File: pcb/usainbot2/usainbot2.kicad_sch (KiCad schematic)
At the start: 13 parts, among them J1 BT_MOD, J2 QTR1-L, J3 QTR1-R, J4 QTR8, J5 SWITCH, M1 Conn_01x02_Male, M2 Conn_01x02_Male, SW1 BTN1, SW2 BTN2

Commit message: update pcb, falta rutear
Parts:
- removed J4: QTR8, Connector_PinSocket_2.54mm:PinSocket_1x11_P2.54mm_Horizontal, symbol usainbot2-rescue:Conn_01x11_Female-Connector
- removed J5: SWITCH, Connector_PinHeader_2.54mm:PinHeader_1x03_P2.54mm_Vertical, symbol usainbot2-rescue:Conn_01x03_Female-Connector
- removed SW1: BTN1, Button_Switch_THT:SW_PUSH_6mm, symbol Switch:SW_MEC_5E
- added C1, C2: C, Capacitor_SMD:C_0805_2012Metric_Pad1.18x1.45mm_HandSolder, symbol Device:C
- added D1: WS2812B, LED_SMD:LED_WS2812B_PLCC4_5.0x5.0mm_P3.2mm, symbol LED:WS2812B
- added J4: QTR-6A, Connector_PinHeader_2.54mm:PinHeader_1x09_P2.54mm_Horizontal, symbol Connector:Conn_01x09_Female
- added SW1: SW_SPDT, usainbot:TOGGLE_RA, symbol Switch:SW_SPDT
- added U2: LM7805_TO220, Package_TO_SOT_THT:TO-220-3_Vertical, symbol Regulator_Linear:LM7805_TO220
- BATTJ6: footprint Connector_PinHeader_2.54mm:PinHeader_1x02_P2.54mm_Horizontal -> Connector_Molex:Molex_KK-254_AE-6410-02A_1x02_P2.54mm_Vertical
- J2, J3: footprint Connector_PinHeader_2.54mm:PinHeader_1x03_P2.54mm_Vertical -> Connector_PinHeader_2.54mm:PinHeader_1x03_P2.54mm_Horizontal
- M1, M2: footprint Connector_PinHeader_2.54mm:PinHeader_1x02_P2.54mm_Horizontal -> Connector_PinHeader_2.54mm:PinHeader_1x02_P2.54mm_Vertical
- U1: value (none) -> TB6612FNG_breakout; footprint (none) -> usainbot:TB6612FNG Breakout
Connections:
- net BTN1 is gone; now on net BTN2: ArduinoNano1.10 (D7)
- net +5V: now also C2.1, J4.8 (Pin_8), U2.3 (VO); no longer ArduinoNano1.27 (+5V)
- net BTN2: no longer ArduinoNano1.11 (D8)
- net GND: now also C1.2, C2.2, D1.3 (VSS), J4.9 (Pin_9), U2.2 (GND)
- net VCC: now also C1.1, SW1.2 (B), U2.1 (VI)
- net at ArduinoNano1.12 (D9): now also D1.4 (DIN)
- net at ArduinoNano1.19 (A0): now also J4.1 (Pin_1)
- net at ArduinoNano1.20 (A1): now also J4.2 (Pin_2)
- net at ArduinoNano1.21 (A2): now also J4.3 (Pin_3)
- net at ArduinoNano1.22 (A3): now also J4.4 (Pin_4)
- net at ArduinoNano1.23 (A4): now also J4.5 (Pin_5)
- net at ArduinoNano1.24 (A5): now also J4.6 (Pin_6)
- net A6: now reaches ArduinoNano1.25 (A6)
- net A6: now also J3.3 (Pin_3)
- net A7: now reaches ArduinoNano1.26 (A7)
- net A7: now also J2.3 (Pin_3)
- net at ArduinoNano1.5 (D2): no longer J2.3 (Pin_3)
- net at ArduinoNano1.6 (D3): no longer J3.3 (Pin_3)
- net at BATTJ6.1 (Pin_1): now also SW1.3 (C)
- new net: ArduinoNano1.27 (+5V), D1.1 (VDD)
- no-connect marks 11 -> 9
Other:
- moved on the sheet: BATTJ6, R0, SW2

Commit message: last pcb update
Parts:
- removed SW2: BTN2, Button_Switch_THT:SW_PUSH_6mm, symbol Switch:SW_MEC_5E
- added SW2: (no value), symbol Switch:SW_Push
- ArduinoNano1: footprint Module:Arduino_Nano -> (none)
- SW1: footprint usainbot:TOGGLE_RA -> (none)
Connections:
- net +5V: now also J2.3 (Pin_3), J3.3 (Pin_3); no longer J2.2 (Pin_2), J3.2 (Pin_2)
- net A6: no longer J3.3 (Pin_3)
- net A7: now also SW2.1; no longer J2.3 (Pin_3)
- net GND: now also SW2.2
- net VCC: now also SW1.3 (C); no longer SW1.2 (B)
- net at ArduinoNano1.13 (D10): now also U1.15 (AIN2); no longer U1.11 (BIN2)
- net at ArduinoNano1.15 (D12): now also U1.11 (BIN2); no longer U1.15 (AIN2)
- net at ArduinoNano1.5 (D2): now also J2.2 (Pin_2)
- net at ArduinoNano1.6 (D3): now also J3.2 (Pin_2)
- net at ArduinoNano1.8 (D5): now also U1.10 (PWMB); no longer U1.16 (PWMA)
- net at ArduinoNano1.9 (D6): now also U1.16 (PWMA); no longer U1.10 (PWMB)
- net at BATTJ6.1 (Pin_1): now also SW1.2 (B); no longer SW1.3 (C)
- net BTN2: no longer names the net of ArduinoNano1.10 (D7)

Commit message: robot racer v2.1 kicad
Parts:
- removed M1, M2: Conn_01x02_Male, Connector_PinHeader_2.54mm:PinHeader_1x02_P2.54mm_Vertical, symbol usainbot2-rescue:Conn_01x02_Male-Connector
- added C3, C4: 0.1u, Capacitor_SMD:C_0805_2012Metric_Pad1.18x1.45mm_HandSolder, symbol Device:C
- added D2: WS2812B, LED_SMD:LED_WS2812B_PLCC4_5.0x5.0mm_P3.2mm, symbol LED:WS2812B
- added J5: M1, Connector_Molex:Molex_KK-254_AE-6410-06A_1x06_P2.54mm_Vertical, symbol Connector:Conn_01x06_Male
- added J7: M2, Connector_Molex:Molex_KK-254_AE-6410-06A_1x06_P2.54mm_Vertical, symbol Connector:Conn_01x06_Male
- added R1: 1K, Resistor_SMD:R_1206_3216Metric_Pad1.30x1.75mm_HandSolder, symbol Device:R_Small_US
- added R2: 2K, Resistor_SMD:R_1206_3216Metric_Pad1.30x1.75mm_HandSolder, symbol Device:R_Small_US
- ArduinoNano1: footprint (none) -> Module:Arduino_Nano
- C1: value C -> 0.22u
- C2: value C -> 0.1u
- SW1: footprint (none) -> usainbot:SPST slide switch
- SW2: value (none) -> SW_Push; footprint (none) -> Button_Switch_SMD:SW_Push_1P1T_NO_Vertical_Wuerth_434133025816
- renumbered BATTJ6 to J6
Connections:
- net A6 is gone; now on an unnamed net: ArduinoNano1.25 (A6)
- net +5V: now also U1.13 (STBY); no longer J1.4 (Pin_4)
- net GND: now also C3.2, C4.2, D2.3 (VSS), J5.6 (Pin_6), J7.6 (Pin_6), R2.2
- net at ArduinoNano1.1 (D1/TX): now also R1.2; no longer J1.1 (Pin_1)
- net D7: now reaches ArduinoNano1.10 (D7)
- net D7: now also SW2.1
- net D8: now reaches ArduinoNano1.11 (D8)
- net D8: now also J7.5 (Pin_5)
- net at J4.1 (Pin_1): now also ArduinoNano1.21 (A2); no longer ArduinoNano1.19 (A0)
- net at J4.2 (Pin_2): now also ArduinoNano1.22 (A3); no longer ArduinoNano1.20 (A1)
- net at J4.3 (Pin_3): now also ArduinoNano1.23 (A4); no longer ArduinoNano1.21 (A2)
- net at J4.4 (Pin_4): now also ArduinoNano1.24 (A5); no longer ArduinoNano1.22 (A3)
- net at J4.5 (Pin_5): no longer ArduinoNano1.23 (A4)
- net at J4.6 (Pin_6): now also ArduinoNano1.26 (A7); no longer ArduinoNano1.24 (A5)
- net +5VD: now reaches ArduinoNano1.27 (+5V), D1.1 (VDD)
- net +5VD: now also J1.4 (Pin_4), C3.1, C4.1, D2.1 (VDD), J5.3 (Pin_3), J7.3 (Pin_3)
- net D2: now reaches ArduinoNano1.5 (D2)
- net D2: now also J5.4 (Pin_4); no longer J2.2 (Pin_2)
- net D3: now reaches ArduinoNano1.6 (D3)
- net D3: now also J7.4 (Pin_4); no longer J3.2 (Pin_2)
- net D4: now reaches ArduinoNano1.7 (D4)
- net D4: now also J5.5 (Pin_5); no longer U1.13 (STBY)
- net ML-2: now reaches U1.5 (AO2)
- net ML-2: now also J5.2 (Pin_2)
- net ML-1: now reaches U1.4 (AO1)
- net ML-1: now also J5.1 (Pin_1)
- net MR-2: now reaches U1.6 (BO2)
- net MR-2: now also J7.2 (Pin_2)
- net MR-1: now reaches U1.7 (BO1)
- net MR-1: now also J7.1 (Pin_1)
- net at D1.2 (DOUT): now also D2.4 (DIN)
- removed net A7: ArduinoNano1.26 (A7), SW2.1
- new net: J1.1 (Pin_1), R1.1, R2.1
- new net QTR-L: ArduinoNano1.19 (A0), J2.2 (Pin_2)
- new net QTR-R: ArduinoNano1.20 (A1), J3.2 (Pin_2)
- no-connect marks 9 -> 7
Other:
- moved on the sheet: J4

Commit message: add led and add top pwrgnd isolation copper
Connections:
- net GND: no longer U1.3 (GND)
- net GNDPWR: now also U1.3 (GND)
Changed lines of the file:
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@@
   (junction (at 241.3 73.66) (diameter 0) (color 0 0 0 0)
+  )
+  (junction (at 76.2 135.89) (diameter 0) (color 0 0 0 0)
   )
   (junction (at 186.69 123.19) (diameter 0) (color 0 0 0 0)
@@
   )
   (wire (pts (xy 69.85 41.91) (xy 69.85 54.61))
+    (stroke (width 0) (type default) (color 0 0 0 0))
+  )
+  (wire (pts (xy 66.04 135.89) (xy 76.2 135.89))
     (stroke (width 0) (type default) (color 0 0 0 0))
   )
@@
     (pin "1")
   )
-  (symbol (lib_id "usainbot2-rescue:GND-power") (at 66.04 135.89 0) (unit 1)
-    (in_bom yes) (on_board yes)
-    (property "Reference" "#PWR0104" (id 0) (at 66.04 142.24 0)
-      (effects (font (size 1.27 1.27)) hide)
-    )
-    (property "Value" "GND" (id 1) (at 66.167 140.2842 0))
-    (property "Footprint" "" (id 2) (at 66.04 135.89 0)
-      (effects (font (size 1.27 1.27)) hide)
-    )
-    (property "Datasheet" "" (id 3) (at 66.04 135.89 0)
-      (effects (font (size 1.27 1.27)) hide)
-    )
-    (pin "1")
-  )
   (symbol (lib_id "usainbot2-rescue:+5V-power") (at 134.62 40.64 0) (unit 1)
     (in_bom yes) (on_board yes)
@@
       (reference "#PWR0103") (unit 1) (value "VCC") (footprint "")
     )
-    (path "/00000000-0000-0000-0000-000062489ac8"
-      (reference "#PWR0104") (unit 1) (value "GND") (footprint "")
-    )
     (path "/0fbe4066-40a9-4e86-906d-3aef413a81c3"

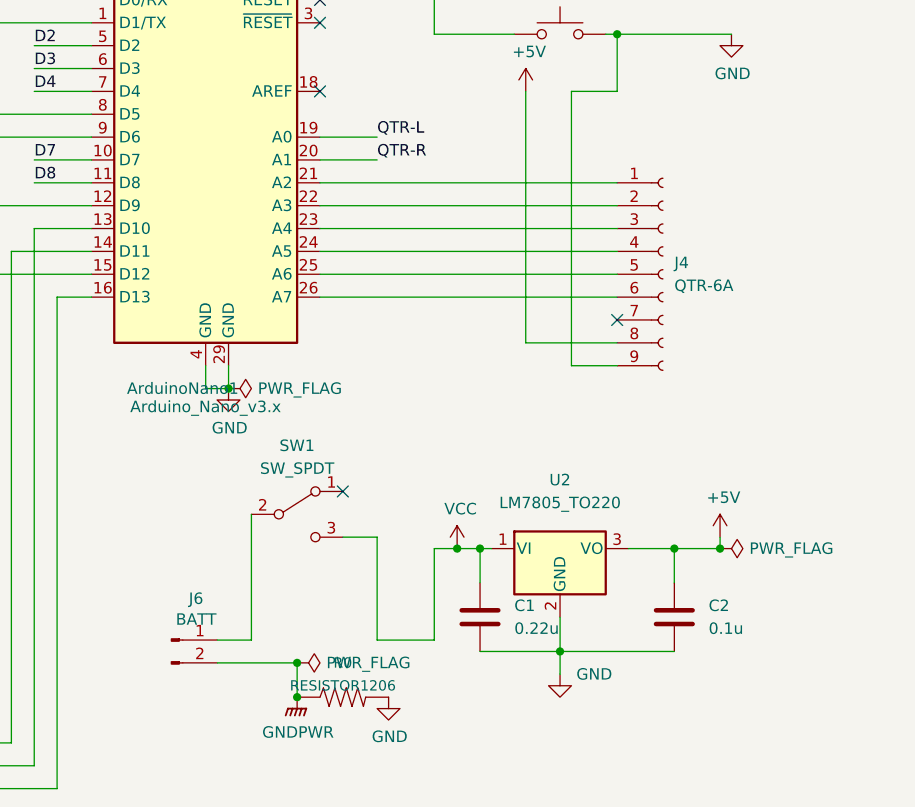
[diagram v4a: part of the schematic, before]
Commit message: add TB6612FNG documentation and update pcb
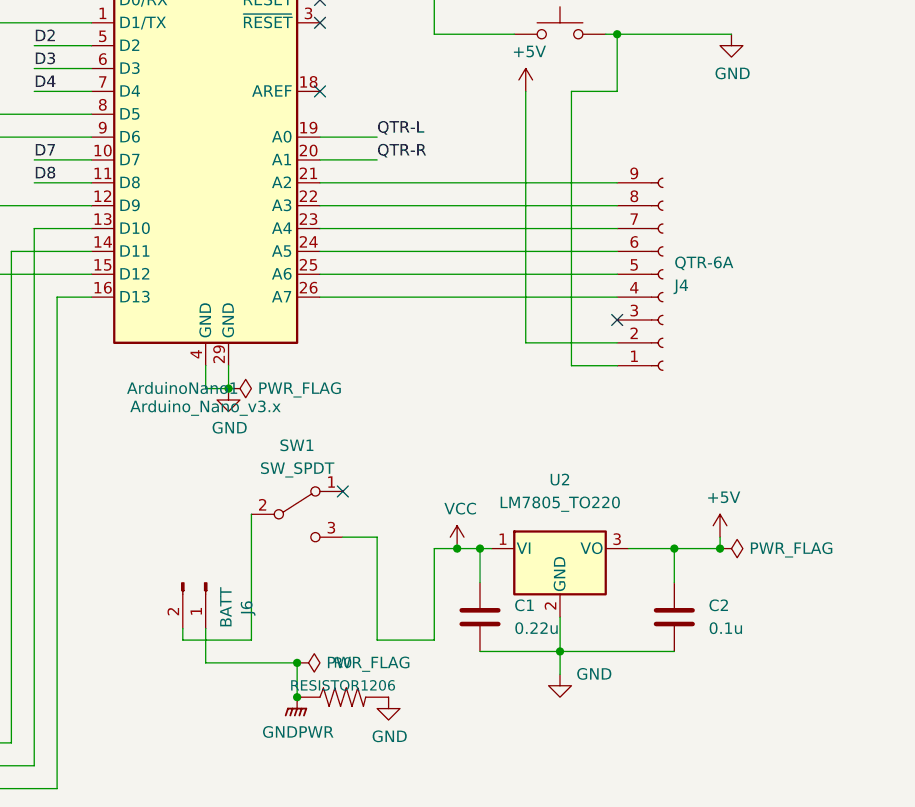
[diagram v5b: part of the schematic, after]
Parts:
- J1: footprint Connector_PinHeader_2.54mm:PinHeader_1x04_P2.54mm_Vertical -> Connector_PinSocket_2.54mm:PinSocket_1x04_P2.54mm_Vertical
- J2, J3: footprint Connector_PinHeader_2.54mm:PinHeader_1x03_P2.54mm_Horizontal -> Connector_PinHeader_2.54mm:PinHeader_1x03_P2.54mm_Vertical
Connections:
- net +5V: now also J4.2 (Pin_2); no longer J4.8 (Pin_8)
- net GND: now also J4.1 (Pin_1); no longer J4.9 (Pin_9)
- net GNDPWR: now also J6.1 (Pin_1); no longer J6.2 (Pin_2)
- net at ArduinoNano1.21 (A2): now also J4.9 (Pin_9); no longer J4.1 (Pin_1)
- net at ArduinoNano1.22 (A3): now also J4.8 (Pin_8); no longer J4.2 (Pin_2)
- net at ArduinoNano1.23 (A4): now also J4.7 (Pin_7); no longer J4.3 (Pin_3)
- net at ArduinoNano1.24 (A5): now also J4.6 (Pin_6); no longer J4.4 (Pin_4)
- net at ArduinoNano1.26 (A7): now also J4.4 (Pin_4); no longer J4.6 (Pin_6)
- net at SW1.2 (B): now also J6.2 (Pin_2); no longer J6.1 (Pin_1)
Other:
- moved on the sheet: J6
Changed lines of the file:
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@@
-    (stroke (width 0) (type default) (color 0 0 0 0))
-  )
-  (wire (pts (xy 130.81 133.35) (xy 134.62 133.35))
     (stroke (width 0) (type default) (color 0 0 0 0))
   )
@@
     (stroke (width 0) (type default) (color 0 0 0 0))
   )
+  (wire (pts (xy 127 133.35) (xy 134.62 133.35))
+    (stroke (width 0) (type default) (color 0 0 0 0))
+  )
   (wire (pts (xy 49.53 113.03) (xy 49.53 149.86))
     (stroke (width 0) (type default) (color 0 0 0 0))
@@
     (stroke (width 0) (type default) (color 0 0 0 0))
   )
+  (wire (pts (xy 127 133.35) (xy 127 132.08))
+    (stroke (width 0) (type default) (color 0 0 0 0))
+  )
   (wire (pts (xy 224.79 90.17) (xy 233.68 90.17))
     (stroke (width 0) (type default) (color 0 0 0 0))
   )
-  (wire (pts (xy 130.81 135.89) (xy 139.7 135.89))
-    (stroke (width 0) (type default) (color 0 0 0 0))
-  )
   (wire (pts (xy 113.03 43.18) (xy 177.8 43.18))
     (stroke (width 0) (type default) (color 0 0 0 0))
   )
+  (wire (pts (xy 129.54 135.89) (xy 139.7 135.89))
+    (stroke (width 0) (type default) (color 0 0 0 0))
+  )
   (wire (pts (xy 168.91 134.62) (xy 181.61 134.62))
     (stroke (width 0) (type default) (color 0 0 0 0))
@@
   )
   (wire (pts (xy 58.42 118.11) (xy 54.61 118.11))
+    (stroke (width 0) (type default) (color 0 0 0 0))
+  )
+  (wire (pts (xy 129.54 132.08) (xy 129.54 135.89))
     (stroke (width 0) (type default) (color 0 0 0 0))
   )
@@
       (effects (font (size 1.27 1.27)) (justify left))
     )
-    (property "Footprint" "Connector_PinHeader_2.54mm:PinHeader_1x03_P2.54mm_Horizontal" (id 2) (at 57.15 44.45 0)
+    (property "Footprint" "Connector_PinHeader_2.54mm:PinHeader_1x03_P2.54mm_Vertical" (id 2) (at 57.15 44.45 0)
       (effects (font (size 1.27 1.27)) hide)
     )
@@
       (effects (font (size 1.27 1.27)) (justify left))
     )
-    (property "Footprint" "Connector_PinHeader_2.54mm:PinHeader_1x03_P2.54mm_Horizontal" (id 2) (at 81.28 44.45 0)
+    (property "Footprint" "Connector_PinHeader_2.54mm:PinHeader_1x03_P2.54mm_Vertical" (id 2) (at 81.28 44.45 0)
       (effects (font (size 1.27 1.27)) hide)
     )
@@
     (pin "1")
   )
-  (symbol (lib_id "usainbot2-rescue:Conn_01x02_Male-Connector") (at 125.73 133.35 0) (unit 1)
-    (in_bom yes) (on_board yes)
-    (property "Reference" "J6" (id 0) (at 128.4732 128.7526 0))
-    (property "Value" "BATT" (id 1) (at 128.4732 131.064 0))
-    (property "Footprint" "Connector_Molex:Molex_KK-254_AE-6410-02A_1x02_P2.54mm_Vertical" (id 2) (at 125.73 133.35 0)
-      (effects (font (size 1.27 1.27)) hide)
-    )
-    (property "Datasheet" "~" (id 3) (at 125.73 133.35 0)
+  (symbol (lib_id "usainbot2-rescue:Conn_01x02_Male-Connector") (at 129.54 127 270) (unit 1)
+    (in_bom yes) (on_board yes)
+    (property "Reference" "J6" (id 0) (at 134.1374 129.7432 0))
+    (property "Value" "BATT" (id 1) (at 131.826 129.7432 0))
+    (property "Footprint" "Connector_Molex:Molex_KK-254_AE-6410-02A_1x02_P2.54mm_Vertical" (id 2) (at 129.54 127 0)
+      (effects (font (size 1.27 1.27)) hide)
+    )
+    (property "Datasheet" "~" (id 3) (at 129.54 127 0)
       (effects (font (size 1.27 1.27)) hide)
     )
@@
       (effects (font (size 1.27 1.27)) (justify right))
     )
-    (property "Footprint" "Connector_PinHeader_2.54mm:PinHeader_1x04_P2.54mm_Vertical" (id 2) (at 97.79 33.02 0)
+    (property "Footprint" "Connector_PinSocket_2.54mm:PinSocket_1x04_P2.54mm_Vertical" (id 2) (at 97.79 33.02 0)
       (effects (font (size 1.27 1.27)) hide)
     )
@@
     (pin "1")
   )
-  (symbol (lib_id "Connector:Conn_01x09_Female") (at 180.34 92.71 0) (unit 1)
-    (in_bom yes) (on_board yes)
-    (property "Reference" "J4" (id 0) (at 181.61 91.4399 0)
-      (effects (font (size 1.27 1.27)) (justify left))
-    )
-    (property "Value" "QTR-6A" (id 1) (at 181.61 93.9799 0)
+  (symbol (lib_id "Connector:Conn_01x09_Female") (at 180.34 92.71 0) (mirror x) (unit 1)
+    (in_bom yes) (on_board yes)
+    (property "Reference" "J4" (id 0) (at 181.61 93.9801 0)
+      (effects (font (size 1.27 1.27)) (justify left))
+    )
+    (property "Value" "QTR-6A" (id 1) (at 181.61 91.4401 0)
       (effects (font (size 1.27 1.27)) (justify left))
     )
@@
     )
     (path "/00000000-0000-0000-0000-0000625be861"
-      (reference "J1") (unit 1) (value "BT_MOD") (footprint "Connector_PinHeader_2.54mm:PinHeader_1x04_P2.54mm_Vertical")
+      (reference "J1") (unit 1) (value "BT_MOD") (footprint "Connector_PinSocket_2.54mm:PinSocket_1x04_P2.54mm_Vertical")
     )
     (path "/00000000-0000-0000-0000-000062464e3e"
-      (reference "J2") (unit 1) (value "QTR1-L") (footprint "Connector_PinHeader_2.54mm:PinHeader_1x03_P2.54mm_Horizontal")
+      (reference "J2") (unit 1) (value "QTR1-L") (footprint "Connector_PinHeader_2.54mm:PinHeader_1x03_P2.54mm_Vertical")
     )
     (path "/00000000-0000-0000-0000-00006246566f"
-      (reference "J3") (unit 1) (value "QTR1-R") (footprint "Connector_PinHeader_2.54mm:PinHeader_1x03_P2.54mm_Horizontal")
+      (reference "J3") (unit 1) (value "QTR1-R") (footprint "Connector_PinHeader_2.54mm:PinHeader_1x03_P2.54mm_Vertical")
     )
     (path "/331fcdc4-1272-4cc4-be96-17ffe2fd6fac"
